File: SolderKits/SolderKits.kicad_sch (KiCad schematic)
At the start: 4 parts, among them SW1 SW_SPST

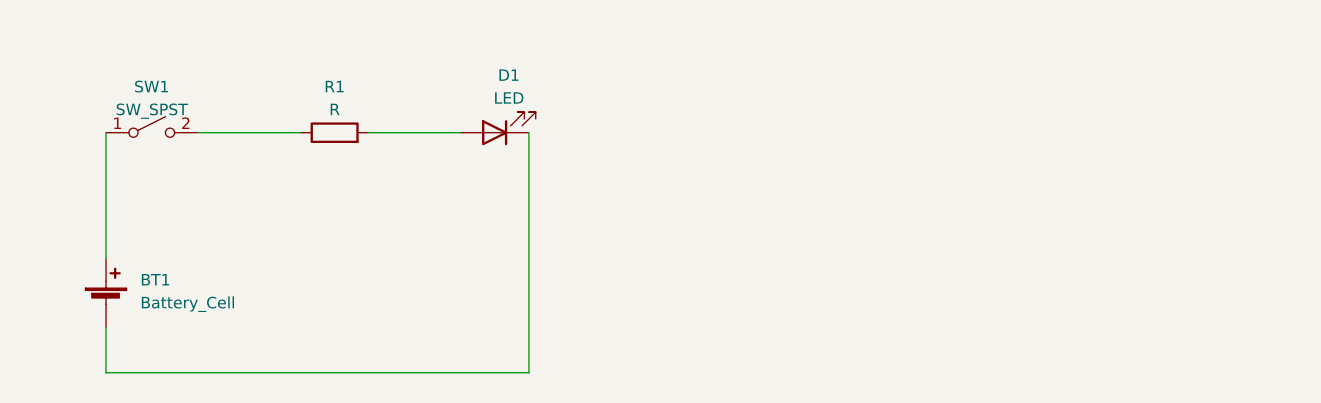
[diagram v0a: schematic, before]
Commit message: adding footprints
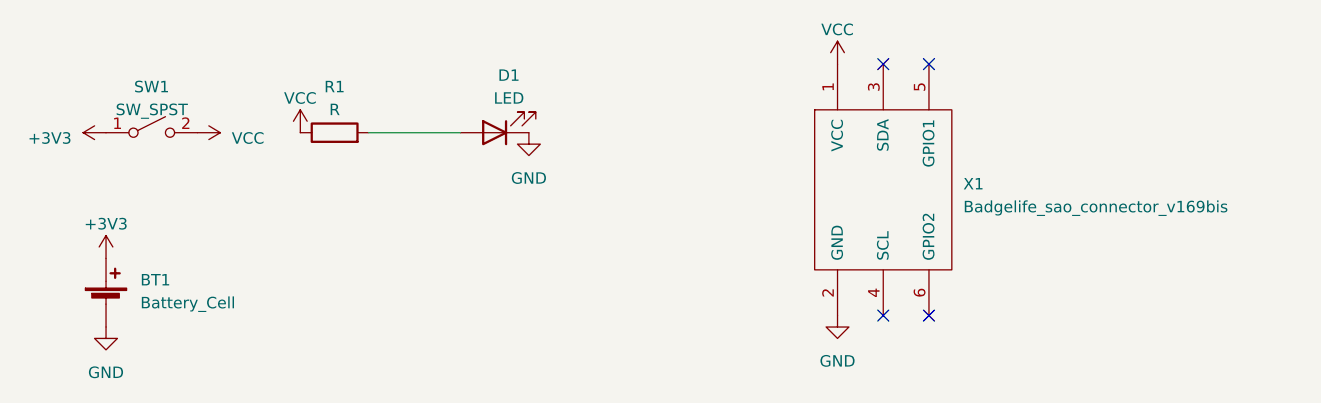
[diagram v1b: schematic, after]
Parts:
- added X1: Badgelife_sao_connector_v169bis, BadgePirates:Badgelife-SAOv169-SAO_Side_B.SLK, symbol BadgePiratesSymbolLibrary:Badgelife_sao_connector_v169bis
- BT1: footprint (none) -> BadgePirates:2032 Through Hold Holder
- D1: footprint (none) -> BadgePirates:LED_D5.0mm
- R1: footprint (none) -> BadgePirates:R_Box_L13.0mm_W4.0mm_P9.00mm
- SW1: footprint (none) -> BadgePirates:SW_Slide_1P2T_CK_TH
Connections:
- net +3V3: now reaches BT1.1 (+), SW1.1 (A)
- net GND: now reaches BT1.2 (-), D1.1 (K)
- net GND: now also X1.2 (GND)
- net VCC: now reaches R1.1, SW1.2 (B)
- net VCC: now also X1.1 (VCC)
- no-connect marks 0 -> 4
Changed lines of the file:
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@@
 (kicad_sch (version 20230121) (generator eeschema)
   (paper "A4")
+  (no_connect (at 189.23 73.66))
+  (no_connect (at 189.23 101.6))
+  (no_connect (at 184.15 73.66))
+  (no_connect (at 184.15 101.6))
   (wire (pts (xy 127 81.28) (xy 137.16 81.28))
     (stroke (width 0) (type default))
   )
-  (wire (pts (xy 97.79 107.95) (xy 97.79 102.87))
-    (stroke (width 0) (type default))
-  )
-  (wire (pts (xy 107.95 81.28) (xy 119.38 81.28))
-    (stroke (width 0) (type default))
-  )
-  (wire (pts (xy 144.78 81.28) (xy 144.78 107.95))
-    (stroke (width 0) (type default))
-  )
-  (wire (pts (xy 144.78 107.95) (xy 97.79 107.95))
-    (stroke (width 0) (type default))
-  )
-  (wire (pts (xy 97.79 81.28) (xy 97.79 95.25))
-    (stroke (width 0) (type default))
+  (symbol (lib_id "power:VCC") (at 107.95 81.28 270) (unit 1)
+    (in_bom yes) (on_board yes) (dnp no) (fields_autoplaced)
+    (property "Reference" "#PWR03" (at 104.14 81.28 0)
+      (effects (font (size 1.27 1.27)) hide)
+    )
+    (property "Value" "VCC" (at 111.76 81.915 90)
+      (effects (font (size 1.27 1.27)) (justify left))
+    )
+    (property "Footprint" "" (at 107.95 81.28 0)
+      (effects (font (size 1.27 1.27)) hide)
+    )
+    (property "Datasheet" "" (at 107.95 81.28 0)
+      (effects (font (size 1.27 1.27)) hide)
+    )
+    (pin "1")
+    (instances
+      (project "SolderKits"
+        (path "/1c79b16c-a7e7-4901-80c8-dae35ec1597a"
+          (reference "#PWR03") (unit 1)
+        )
+      )
+    )
   )
   (symbol (lib_id "Device:Battery_Cell") (at 97.79 100.33 0) (unit 1)
@@
       (effects (font (size 1.27 1.27)) (justify left))
     )
-    (property "Footprint" "" (at 97.79 98.806 90)
+    (property "Footprint" "BadgePirates:2032 Through Hold Holder" (at 97.79 98.806 90)
       (effects (font (size 1.27 1.27)) hide)
     )
@@
       (effects (font (size 1.27 1.27)))
     )
-    (property "Footprint" "" (at 123.19 83.058 90)
+    (property "Footprint" "BadgePirates:R_Box_L13.0mm_W4.0mm_P9.00mm" (at 123.19 83.058 90)
       (effects (font (size 1.27 1.27)) hide)
     )
@@
     )
   )
+  (symbol (lib_id "power:+3V3") (at 97.79 81.28 90) (unit 1)
+    (in_bom yes) (on_board yes) (dnp no) (fields_autoplaced)
+    (property "Reference" "#PWR02" (at 101.6 81.28 0)
+      (effects (font (size 1.27 1.27)) hide)
+    )
+    (property "Value" "+3V3" (at 93.98 81.915 90)
+      (effects (font (size 1.27 1.27)) (justify left))
+    )
+    (property "Footprint" "" (at 97.79 81.28 0)
+      (effects (font (size 1.27 1.27)) hide)
+    )
+    (property "Datasheet" "" (at 97.79 81.28 0)
+      (effects (font (size 1.27 1.27)) hide)
+    )
+    (pin "1")
+    (instances
+      (project "SolderKits"
+        (path "/1c79b16c-a7e7-4901-80c8-dae35ec1597a"
+          (reference "#PWR02") (unit 1)
+        )
+      )
+    )
+  )
+  (symbol (lib_id "power:VCC") (at 119.38 81.28 0) (unit 1)
+    (in_bom yes) (on_board yes) (dnp no) (fields_autoplaced)
+    (property "Reference" "#PWR04" (at 119.38 85.09 0)
+      (effects (font (size 1.27 1.27)) hide)
+    )
+    (property "Value" "VCC" (at 119.38 77.47 0)
+      (effects (font (size 1.27 1.27)))
+    )
+    (property "Footprint" "" (at 119.38 81.28 0)
+      (effects (font (size 1.27 1.27)) hide)
+    )
+    (property "Datasheet" "" (at 119.38 81.28 0)
+      (effects (font (size 1.27 1.27)) hide)
+    )
+    (pin "1")
+    (instances
+      (project "SolderKits"
+        (path "/1c79b16c-a7e7-4901-80c8-dae35ec1597a"
+          (reference "#PWR04") (unit 1)
+        )
+      )
+    )
+  )
+  (symbol (lib_id "power:GND") (at 97.79 102.87 0) (unit 1)
+    (in_bom yes) (on_board yes) (dnp no) (fields_autoplaced)
+    (property "Reference" "#PWR06" (at 97.79 109.22 0)
+      (effects (font (size 1.27 1.27)) hide)
+    )
+    (property "Value" "GND" (at 97.79 107.95 0)
+      (effects (font (size 1.27 1.27)))
+    )
+    (property "Footprint" "" (at 97.79 102.87 0)
+      (effects (font (size 1.27 1.27)) hide)
+    )
+    (property "Datasheet" "" (at 97.79 102.87 0)
+      (effects (font (size 1.27 1.27)) hide)
+    )
+    (pin "1")
+    (instances
+      (project "SolderKits"
+        (path "/1c79b16c-a7e7-4901-80c8-dae35ec1597a"
+          (reference "#PWR06") (unit 1)
+        )
+      )
+    )
+  )
   (symbol (lib_id "Device:LED") (at 140.97 81.28 180) (unit 1)
     (in_bom yes) (on_board yes) (dnp no) (fields_autoplaced)
@@
       (effects (font (size 1.27 1.27)))
     )
-    (property "Footprint" "" (at 140.97 81.28 0)
+    (property "Footprint" "BadgePirates:LED_D5.0mm" (at 140.97 81.28 0)
       (effects (font (size 1.27 1.27)) hide)
     )
@@
       (effects (font (size 1.27 1.27)))
     )
-    (property "Footprint" "" (at 102.87 81.28 0)
+    (property "Footprint" "BadgePirates:SW_Slide_1P2T_CK_TH" (at 102.87 81.28 0)
       (effects (font (size 1.27 1.27)) hide)
     )
@@
         )
       )
+    )
+  )
+  (symbol (lib_id "power:GND") (at 179.07 101.6 0) (unit 1)
+    (in_bom yes) (on_board yes) (dnp no) (fields_autoplaced)
+    (property "Reference" "#PWR08" (at 179.07 107.95 0)
+      (effects (font (size 1.27 1.27)) hide)
+    )
+    (property "Value" "GND" (at 179.07 106.68 0)
+      (effects (font (size 1.27 1.27)))
+    )
+    (property "Footprint" "" (at 179.07 101.6 0)
+      (effects (font (size 1.27 1.27)) hide)
+    )
+    (property "Datasheet" "" (at 179.07 101.6 0)
+      (effects (font (size 1.27 1.27)) hide)
+    )
+    (pin "1")
+    (instances
+      (project "SolderKits"
+        (path "/1c79b16c-a7e7-4901-80c8-dae35ec1597a"
+          (reference "#PWR08") (unit 1)
+        )
+      )
+    )
+  )
+  (symbol (lib_id "power:GND") (at 144.78 81.28 0) (unit 1)
+    (in_bom yes) (on_board yes) (dnp no) (fields_autoplaced)
+    (property "Reference" "#PWR07" (at 144.78 87.63 0)
+      (effects (font (size 1.27 1.27)) hide)
+    )
+    (property "Value" "GND" (at 144.78 86.36 0)
+      (effects (font (size 1.27 1.27)))
+    )
+    (property "Footprint" "" (at 144.78 81.28 0)
+      (effects (font (size 1.27 1.27)) hide)
+    )
+    (property "Datasheet" "" (at 144.78 81.28 0)
+      (effects (font (size 1.27 1.27)) hide)
+    )
+    (pin "1")
+    (instances
+      (project "SolderKits"
+        (path "/1c79b16c-a7e7-4901-80c8-dae35ec1597a"
+          (reference "#PWR07") (unit 1)
+        )
+      )
+    )
+  )
+  (symbol (lib_id "power:+3V3") (at 97.79 95.25 0) (unit 1)
+    (in_bom yes) (on_board yes) (dnp no) (fields_autoplaced)
+    (property "Reference" "#PWR01" (at 97.79 99.06 0)
+      (effects (font (size 1.27 1.27)) hide)
+    )
+    (property "Value" "+3V3" (at 97.79 91.44 0)
+      (effects (font (size 1.27 1.27)))
+    )
+    (property "Footprint" "" (at 97.79 95.25 0)
+      (effects (font (size 1.27 1.27)) hide)
+    )
+    (property "Datasheet" "" (at 97.79 95.25 0)
+      (effects (font (size 1.27 1.27)) hide)
+    )
+    (pin "1")
+    (instances
+      (project "SolderKits"
+        (path "/1c79b16c-a7e7-4901-80c8-dae35ec1597a"
+          (reference "#PWR01") (unit 1)
+        )
+      )
+    )
+  )
+  (symbol (lib_id "BadgePiratesSymbolLibrary:Badgelife_sao_connector_v169bis") (at 184.15 87.63 0) (unit 1)
+    (in_bom yes) (on_board yes) (dnp no) (fields_autoplaced)
+    (property "Reference" "X1" (at 193.04 86.995 0)
+      (effects (font (size 1.27 1.27)) (justify left))
+    )
+    (property "Value" "Badgelife_sao_connector_v169bis" (at 193.04 89.535 0)
+      (effects (font (size 1.27 1.27)) (justify left))
+    )
+    (property "Footprint" "BadgePirates:Badgelife-SAOv169-SAO_Side_B.SLK" (at 184.15 82.55 0)
+      (effects (font (size 1.27 1.27)) hide)
+    )
+    (property "Datasheet" "" (at 184.15 82.55 0)
+      (effects (font (size 1.27 1.27)) hide)
+    )
+    (pin "1")
+    (pin "2")
+    (pin "3")
+    (pin "4")
+    (pin "5")
+    (pin "6")
+    (instances
+      (project "SolderKits"
+        (path "/1c79b16c-a7e7-4901-80c8-dae35ec1597a"
+          (reference "X1") (unit 1)
+        )
+      )
+    )
+  )
+  (symbol (lib_id "power:VCC") (at 179.07 73.66 0) (unit 1)
+    (in_bom yes) (on_board yes) (dnp no) (fields_autoplaced)
+    (property "Reference" "#PWR05" (at 179.07 77.47 0)
+      (effects (font (size 1.27 1.27)) hide)
+    )
+    (property "Value" "VCC" (at 179.07 69.85 0)
+      (effects (font (size 1.27 1.27)))
+    )
+    (property "Footprint" "" (at 179.07 73.66 0)
+      (effects (font (size 1.27 1.27)) hide)
+    )
+    (property "Datasheet" "" (at 179.07 73.66 0)
+      (effects (font (size 1.27 1.27)) hide)
+    )
+    (pin "1")
+    (instances
+      (project "SolderKits"
+        (path "/1c79b16c-a7e7-4901-80c8-dae35ec1597a"
+          (reference "#PWR05") (unit 1)
+        )
+      )
